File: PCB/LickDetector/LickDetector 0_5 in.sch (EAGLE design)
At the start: 9 parts, among them IC1 74AHC1G14DBV, J1 AUDIO_JACK_3.5MM_PTH, Q1 SFH_3015_FA

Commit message: Added power and signal LEDs to Lick Detector beam break PCB
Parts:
- added PWR, SIG: (no value), led:LEDCHIP-LED0603
- added R3, R4: (no value), resistor:R-US_R0603
- IC1: value 74AHC1G14DBV -> 74AHC1G14DCK; device 74xx-little-de:74AHC1G14DBV -> 74xx-little-de:74AHC1G14DCK
- R1, R2: device rcl:R-US_R0603 -> resistor:R-US_R0603
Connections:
- new net N$1: PWR.A, R3.2
- new net N$2: R4.2, SIG.A
- net GND: now also PWR.C, SIG.C
- net SIGNAL: now also R4.1
- net VCC: now also R3.1
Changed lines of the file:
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@@
 <?xml version="1.0" encoding="utf-8"?>
 <!DOCTYPE eagle SYSTEM "eagle.dtd">
-<eagle version="9.4.0">
+<eagle version="9.4.2">
 <drawing>
 <settings>
@@
 <part name="LED1" library="led" library_urn="urn:adsk.eagle:library:259" deviceset="LED" device="CHIPLED_1206" package3d_urn="urn:adsk.eagle:package:15823/2"/>
 <part name="Q1" library="SFH_3015_FA" deviceset="SFH_3015_FA" device=""/>
-<part name="IC1" library="74xx-little-de" library_urn="urn:adsk.eagle:library:86" deviceset="74*1G14" device="DBV" package3d_urn="urn:adsk.eagle:package:2406/2" technology="AHC"/>
+<part name="IC1" library="74xx-little-de" library_urn="urn:adsk.eagle:library:86" deviceset="74*1G14" device="DCK" package3d_urn="urn:adsk.eagle:package:2405/2" technology="AHC" value="74AHC1G14DCK"/>
 <part name="GND1" library="supply1" library_urn="urn:adsk.eagle:library:371" deviceset="GND" device=""/>
 <part name="GND2" library="supply1" library_urn="urn:adsk.eagle:library:371" deviceset="GND" device=""/>
 <part name="P+1" library="supply1" library_urn="urn:adsk.eagle:library:371" deviceset="VCC" device=""/>
 <part name="P+2" library="supply1" library_urn="urn:adsk.eagle:library:371" deviceset="VCC" device=""/>
-<part name="R1" library="rcl" library_urn="urn:adsk.eagle:library:334" deviceset="R-US_" device="R0603" package3d_urn="urn:adsk.eagle:package:23555/3"/>
-<part name="R2" library="rcl" library_urn="urn:adsk.eagle:library:334" deviceset="R-US_" device="R0603" package3d_urn="urn:adsk.eagle:package:23555/3"/>
+<part name="R1" library="resistor" library_urn="urn:adsk.eagle:library:348" deviceset="R-US_" device="R0603" package3d_urn="urn:adsk.eagle:package:23555/3"/>
+<part name="R2" library="resistor" library_urn="urn:adsk.eagle:library:348" deviceset="R-US_" device="R0603" package3d_urn="urn:adsk.eagle:package:23555/3"/>
 <part name="SV1" library="con-lstb" library_urn="urn:adsk.eagle:library:162" deviceset="MA03-1" device="" package3d_urn="urn:adsk.eagle:package:8339/1"/>
 <part name="J1" library="SparkFun-Connectors" library_urn="urn:adsk.eagle:library:513" deviceset="AUDIO_JACK_3.5MM" device="_PTH" package3d_urn="urn:adsk.eagle:package:37997/1"/>
 <part name="J2" library="SparkFun-Connectors" library_urn="urn:adsk.eagle:library:513" deviceset="CONN_02" device="" package3d_urn="urn:adsk.eagle:package:38039/1"/>
 <part name="J3" library="SparkFun-Connectors" library_urn="urn:adsk.eagle:library:513" deviceset="CONN_02" device="" package3d_urn="urn:adsk.eagle:package:38039/1"/>
+<part name="R3" library="resistor" library_urn="urn:adsk.eagle:library:348" deviceset="R-US_" device="R0603" package3d_urn="urn:adsk.eagle:package:23555/3"/>
+<part name="R4" library="resistor" library_urn="urn:adsk.eagle:library:348" deviceset="R-US_" device="R0603" package3d_urn="urn:adsk.eagle:package:23555/3"/>
+<part name="PWR" library="led" library_urn="urn:adsk.eagle:library:259" deviceset="LED" device="CHIP-LED0603" package3d_urn="urn:adsk.eagle:package:15819/3"/>
+<part name="SIG" library="led" library_urn="urn:adsk.eagle:library:259" deviceset="LED" device="CHIP-LED0603" package3d_urn="urn:adsk.eagle:package:15819/3"/>
+<part name="GND3" library="supply1" library_urn="urn:adsk.eagle:library:371" deviceset="GND" device=""/>
+<part name="GND4" library="supply1" library_urn="urn:adsk.eagle:library:371" deviceset="GND" device=""/>
 </parts>
 <sheets>
@@
 <attribute name="NAME" x="71.12" y="4.572" size="1.778" layer="95" font="vector" rot="R180"/>
 </instance>
+<instance part="R3" gate="G$1" x="25.4" y="81.28" smashed="yes">
+<attribute name="NAME" x="21.59" y="82.7786" size="1.778" layer="95"/>
+<attribute name="VALUE" x="21.59" y="77.978" size="1.778" layer="96"/>
+</instance>
+<instance part="R4" gate="G$1" x="63.5" y="81.28" smashed="yes">
+<attribute name="NAME" x="59.69" y="82.7786" size="1.778" layer="95"/>
+<attribute name="VALUE" x="59.69" y="77.978" size="1.778" layer="96"/>
+</instance>
+<instance part="PWR" gate="G$1" x="35.56" y="81.28" smashed="yes" rot="R90">
+<attribute name="NAME" x="40.132" y="84.836" size="1.778" layer="95" rot="R180"/>
+<attribute name="VALUE" x="40.132" y="86.995" size="1.778" layer="96" rot="R180"/>
+</instance>
+<instance part="SIG" gate="G$1" x="73.66" y="81.28" smashed="yes" rot="R90">
+<attribute name="NAME" x="78.232" y="84.836" size="1.778" layer="95" rot="R180"/>
+<attribute name="VALUE" x="78.232" y="86.995" size="1.778" layer="96" rot="R180"/>
+</instance>
+<instance part="GND3" gate="1" x="82.55" y="72.39" smashed="yes">
+<attribute name="VALUE" x="80.01" y="69.85" size="1.778" layer="96"/>
+</instance>
+<instance part="GND4" gate="1" x="44.45" y="72.39" smashed="yes">
+<attribute name="VALUE" x="41.91" y="69.85" size="1.778" layer="96"/>
+</instance>
 </instances>
 <busses>
@@
 <label x="48.26" y="10.16" size="1.778" layer="95"/>
 </segment>
+<segment>
+<pinref part="R3" gate="G$1" pin="1"/>
+<wire x1="20.32" y1="81.28" x2="12.7" y2="81.28" width="0.1524" layer="91"/>
+<label x="12.7" y="81.28" size="1.778" layer="95"/>
+</segment>
 </net>
 <net name="GND" class="0">
@@
 <wire x1="20.32" y1="12.7" x2="2.54" y2="12.7" width="0.1524" layer="91"/>
 <label x="2.54" y="12.7" size="1.778" layer="95"/>
+</segment>
+<segment>
+<pinref part="GND4" gate="1" pin="GND"/>
+<pinref part="PWR" gate="G$1" pin="C"/>
+<wire x1="44.45" y1="74.93" x2="44.45" y2="81.28" width="0.1524" layer="91"/>
+<wire x1="44.45" y1="81.28" x2="40.64" y2="81.28" width="0.1524" layer="91"/>
+</segment>
+<segment>
+<pinref part="GND3" gate="1" pin="GND"/>
+<pinref part="SIG" gate="G$1" pin="C"/>
+<wire x1="82.55" y1="74.93" x2="82.55" y2="81.28" width="0.1524" layer="91"/>
+<wire x1="82.55" y1="81.28" x2="78.74" y2="81.28" width="0.1524" layer="91"/>
 </segment>
 </net>
@@
 <label x="93.218" y="57.658" size="1.778" layer="95" rot="R180"/>
 </segment>
+<segment>
+<pinref part="R4" gate="G$1" pin="1"/>
+<wire x1="58.42" y1="81.28" x2="50.8" y2="81.28" width="0.1524" layer="91"/>
+<label x="50.8" y="81.28" size="1.778" layer="95"/>
+</segment>
 </net>
 <net name="LEDCATHODE" class="0">
@@
 <wire x1="20.32" y1="10.16" x2="2.54" y2="10.16" width="0.1524" layer="91"/>
 <label x="2.54" y="7.62" size="1.778" layer="95"/>
+</segment>
+</net>
+<net name="N$1" class="0">
+<segment>
+<pinref part="PWR" gate="G$1" pin="A"/>
+<pinref part="R3" gate="G$1" pin="2"/>
+<wire x1="33.02" y1="81.28" x2="30.48" y2="81.28" width="0.1524" layer="91"/>
+</segment>
+</net>
+<net name="N$2" class="0">
+<segment>
+<pinref part="SIG" gate="G$1" pin="A"/>
+<pinref part="R4" gate="G$1" pin="2"/>
+<wire x1="71.12" y1="81.28" x2="68.58" y2="81.28" width="0.1524" layer="91"/>
 </segment>
 </net>
@@
 packages will not be understood (or retained) with this version.
 </note>
-<note version="8.4" severity="warning">
-Since Version 8.4, EAGLE supports properties for SPICE simulation.
-Probes in schematics and SPICE mapping objects found in parts and library devices
-will not be understood with this version. Update EAGLE to the latest version
-for full support of SPICE simulation.
-</note>
 </compatibility>

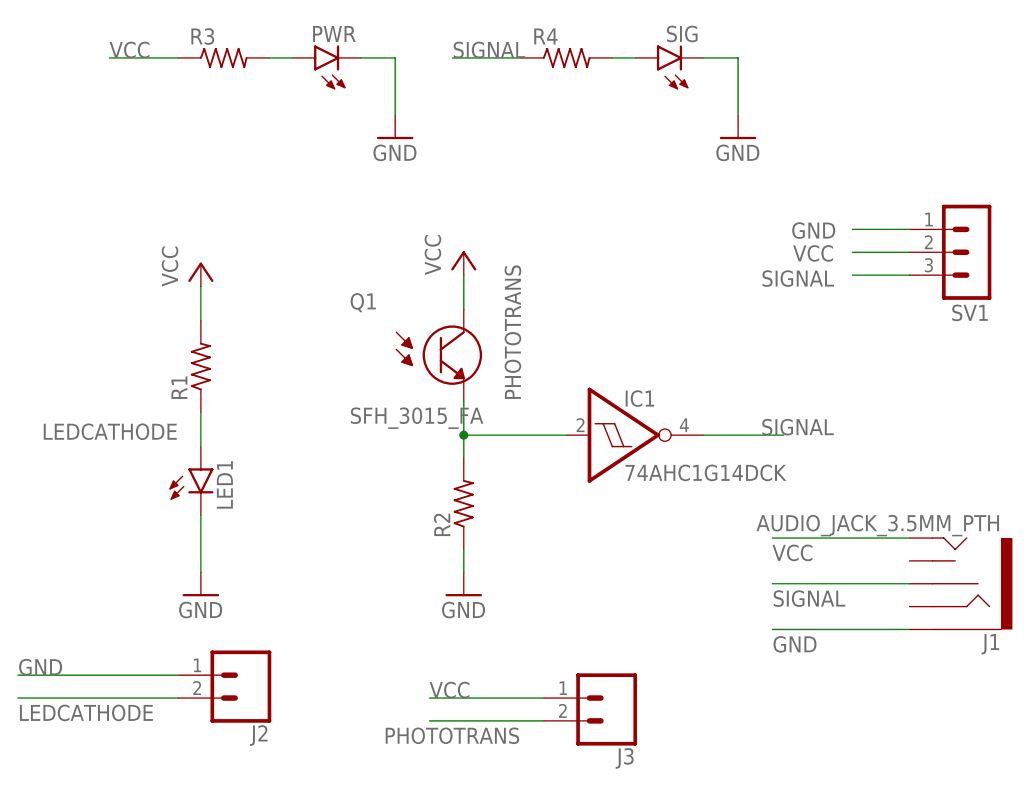
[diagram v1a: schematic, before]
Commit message: Fixed bug where wrong audio jack pin was connected for signal. Also added cuttout for jack and potentiometer
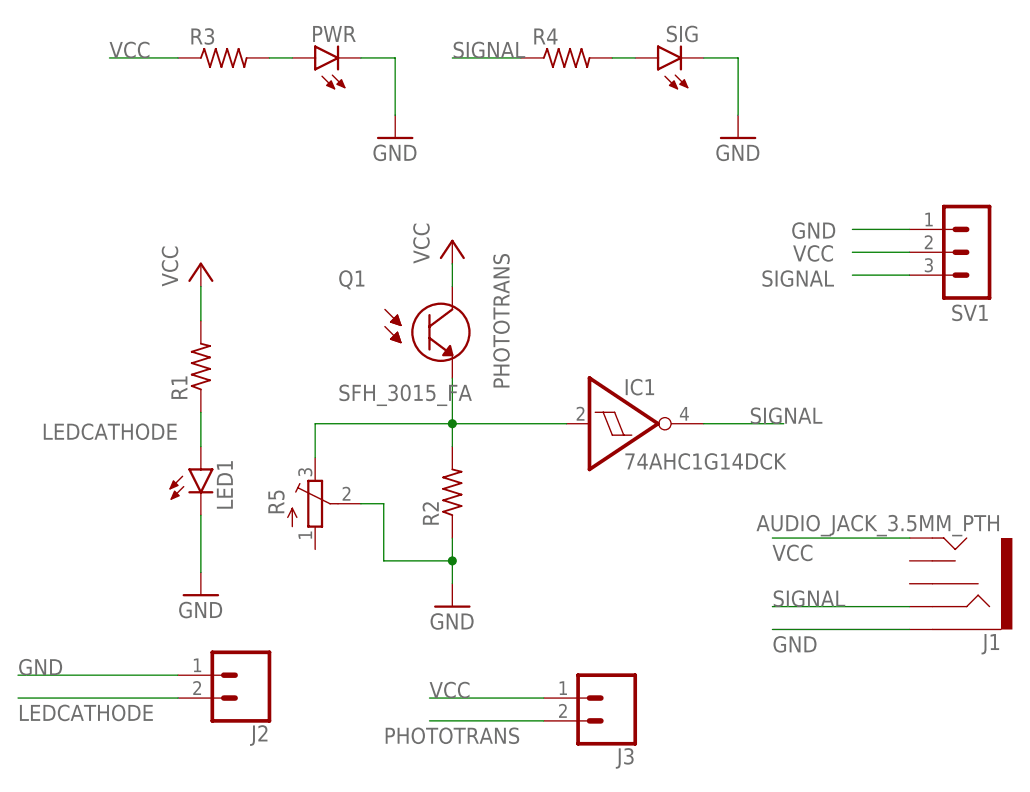
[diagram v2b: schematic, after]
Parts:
- added R5: (no value), pot:TRIM_EU-3223J
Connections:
- net GND: now also R5.S
- net PHOTOTRANS: now also R5.E
- net SIGNAL: now also J1.RING; no longer J1.RSH
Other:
- moved on the sheet: IC1, Q1, R2
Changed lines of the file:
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@@
 <?xml version="1.0" encoding="utf-8"?>
 <!DOCTYPE eagle SYSTEM "eagle.dtd">
-<eagle version="9.4.2">
+<eagle version="9.6.0">
 <drawing>
 <settings>
@@
 <setting verticaltext="up"/>
 </settings>
-<grid distance="0.1" unitdist="inch" unit="inch" style="lines" multiple="1" display="no" altdistance="0.01" altunitdist="inch" altunit="inch"/>
+<grid distance="0.05" unitdist="inch" unit="inch" style="lines" multiple="2" display="yes" altdistance="0.01" altunitdist="inch" altunit="inch"/>
 <layers>
 <layer number="1" name="Top" color="4" fill="1" visible="no" active="no"/>
@@
 <part name="GND3" library="supply1" library_urn="urn:adsk.eagle:library:371" deviceset="GND" device=""/>
 <part name="GND4" library="supply1" library_urn="urn:adsk.eagle:library:371" deviceset="GND" device=""/>
+<part name="R5" library="pot" library_urn="urn:adsk.eagle:library:331" deviceset="TRIM_EU-" device="3223J" package3d_urn="urn:adsk.eagle:package:22724/1"/>
 </parts>
 <sheets>
@@
 <attribute name="VALUE" x="28.575" y="30.988" size="1.778" layer="96" rot="R90"/>
 </instance>
-<instance part="Q1" gate="G$1" x="49.53" y="48.26" smashed="yes">
-<attribute name="NAME" x="39.3744" y="53.3422" size="1.779540625" layer="95"/>
-<attribute name="VALUE" x="39.3792" y="40.64" size="1.78121875" layer="96"/>
-</instance>
-<instance part="IC1" gate="A" x="68.58" y="39.37" smashed="yes">
-<attribute name="NAME" x="69.85" y="42.545" size="1.778" layer="95"/>
-<attribute name="VALUE" x="69.85" y="34.29" size="1.778" layer="96"/>
+<instance part="Q1" gate="G$1" x="48.26" y="50.8" smashed="yes">
+<attribute name="NAME" x="38.1044" y="55.8822" size="1.779540625" layer="95"/>
+<attribute name="VALUE" x="38.1092" y="43.18" size="1.78121875" layer="96"/>
+</instance>
+<instance part="IC1" gate="A" x="68.58" y="40.64" smashed="yes">
+<attribute name="NAME" x="69.85" y="43.815" size="1.778" layer="95"/>
+<attribute name="VALUE" x="69.85" y="35.56" size="1.778" layer="96"/>
 </instance>
 <instance part="GND1" gate="1" x="22.86" y="21.59" smashed="yes">
 <attribute name="VALUE" x="20.32" y="19.05" size="1.778" layer="96"/>
 </instance>
-<instance part="GND2" gate="1" x="52.07" y="21.59" smashed="yes">
-<attribute name="VALUE" x="49.53" y="19.05" size="1.778" layer="96"/>
+<instance part="GND2" gate="1" x="50.8" y="20.32" smashed="yes">
+<attribute name="VALUE" x="48.26" y="17.78" size="1.778" layer="96"/>
 </instance>
 <instance part="P+1" gate="VCC" x="22.86" y="58.42" smashed="yes">
 <attribute name="VALUE" x="20.32" y="55.88" size="1.778" layer="96" rot="R90"/>
 </instance>
-<instance part="P+2" gate="VCC" x="52.07" y="59.69" smashed="yes">
-<attribute name="VALUE" x="49.53" y="57.15" size="1.778" layer="96" rot="R90"/>
+<instance part="P+2" gate="VCC" x="50.8" y="60.96" smashed="yes">
+<attribute name="VALUE" x="48.26" y="58.42" size="1.778" layer="96" rot="R90"/>
 </instance>
 <instance part="R1" gate="G$1" x="22.86" y="46.99" smashed="yes" rot="R90">
@@
 <attribute name="VALUE" x="26.162" y="43.18" size="1.778" layer="96" rot="R90"/>
 </instance>
-<instance part="R2" gate="G$1" x="52.07" y="31.75" smashed="yes" rot="R90">
-<attribute name="NAME" x="50.5714" y="27.94" size="1.778" layer="95" rot="R90"/>
-<attribute name="VALUE" x="55.372" y="27.94" size="1.778" layer="96" rot="R90"/>
+<instance part="R2" gate="G$1" x="50.8" y="33.02" smashed="yes" rot="R90">
+<attribute name="NAME" x="49.3014" y="29.21" size="1.778" layer="95" rot="R90"/>
+<attribute name="VALUE" x="54.102" y="29.21" size="1.778" layer="96" rot="R90"/>
 </instance>
 <instance part="SV1" gate="G$1" x="109.22" y="59.69" smashed="yes" rot="R180">
@@
 <instance part="GND4" gate="1" x="44.45" y="72.39" smashed="yes">
 <attribute name="VALUE" x="41.91" y="69.85" size="1.778" layer="96"/>
+</instance>
+<instance part="R5" gate="1" x="35.56" y="31.75" smashed="yes">
+<attribute name="NAME" x="32.131" y="30.48" size="1.778" layer="95" rot="R90"/>
+<attribute name="VALUE" x="31.75" y="27.94" size="1.778" layer="96" rot="R90"/>
 </instance>
 </instances>
@@
 <pinref part="Q1" gate="G$1" pin="C"/>
 <pinref part="P+2" gate="VCC" pin="VCC"/>
-<wire x1="52.07" y1="57.15" x2="52.07" y2="53.34" width="0.1524" layer="91"/>
+<wire x1="50.8" y1="58.42" x2="50.8" y2="55.88" width="0.1524" layer="91"/>
 </segment>
 <segment>
@@
 <pinref part="R2" gate="G$1" pin="1"/>
 <pinref part="GND2" gate="1" pin="GND"/>
-<wire x1="52.07" y1="24.13" x2="52.07" y2="26.67" width="0.1524" layer="91"/>
+<wire x1="50.8" y1="22.86" x2="50.8" y2="25.4" width="0.1524" layer="91"/>
+<pinref part="R5" gate="1" pin="S"/>
+<wire x1="50.8" y1="25.4" x2="50.8" y2="27.94" width="0.1524" layer="91"/>
+<wire x1="40.64" y1="31.75" x2="43.18" y2="31.75" width="0.1524" layer="91"/>
+<wire x1="43.18" y1="31.75" x2="43.18" y2="25.4" width="0.1524" layer="91"/>
+<wire x1="50.8" y1="25.4" x2="43.18" y2="25.4" width="0.1524" layer="91"/>
+<junction x="50.8" y="25.4"/>
 </segment>
 <segment>
@@
 <pinref part="R2" gate="G$1" pin="2"/>
 <pinref part="Q1" gate="G$1" pin="E"/>
-<wire x1="52.07" y1="43.18" x2="52.07" y2="39.37" width="0.1524" layer="91"/>
-<wire x1="52.07" y1="39.37" x2="52.07" y2="36.83" width="0.1524" layer="91"/>
-<wire x1="52.07" y1="39.37" x2="63.5" y2="39.37" width="0.1524" layer="91"/>
-<junction x="52.07" y="39.37"/>
+<wire x1="50.8" y1="45.72" x2="50.8" y2="40.64" width="0.1524" layer="91"/>
+<wire x1="50.8" y1="40.64" x2="50.8" y2="38.1" width="0.1524" layer="91"/>
+<wire x1="50.8" y1="40.64" x2="63.5" y2="40.64" width="0.1524" layer="91"/>
+<junction x="50.8" y="40.64"/>
 <pinref part="IC1" gate="A" pin="I"/>
-<label x="58.42" y="43.18" size="1.778" layer="95" rot="R90"/>
+<label x="57.15" y="44.45" size="1.778" layer="95" rot="R90"/>
+<pinref part="R5" gate="1" pin="E"/>
+<wire x1="35.56" y1="36.83" x2="35.56" y2="40.64" width="0.1524" layer="91"/>
+<wire x1="35.56" y1="40.64" x2="50.8" y2="40.64" width="0.1524" layer="91"/>
 </segment>
 <segment>
@@
 <segment>
 <pinref part="IC1" gate="A" pin="O"/>
-<wire x1="78.74" y1="39.37" x2="87.63" y2="39.37" width="0.1524" layer="91"/>
-<label x="85.09" y="39.37" size="1.778" layer="95"/>
-</segment>
-<segment>
-<pinref part="J1" gate="G$1" pin="RSH"/>
-<wire x1="101.6" y1="22.86" x2="86.36" y2="22.86" width="0.1524" layer="91"/>
-<label x="86.36" y="20.32" size="1.778" layer="95"/>
+<wire x1="78.74" y1="40.64" x2="87.63" y2="40.64" width="0.1524" layer="91"/>
+<label x="83.82" y="40.64" size="1.778" layer="95"/>
 </segment>
 <segment>
@@
 <label x="50.8" y="81.28" size="1.778" layer="95"/>
 </segment>
+<segment>
+<pinref part="J1" gate="G$1" pin="RING"/>
+<wire x1="101.6" y1="20.32" x2="86.36" y2="20.32" width="0.1524" layer="91"/>
+<label x="86.36" y="20.32" size="1.778" layer="95"/>
+</segment>
 </net>
